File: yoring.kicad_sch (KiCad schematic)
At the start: 41 parts, among them J1 USB-C_USB4105-GF-A, J2 Conn_01x04_Pin, SW1 SW_MEC_5G, U1 ESP32C3, U2 IS25LP016D-JLLE, U4 ICM-20602, U4 USBLC6-2SC6, U5 ICM-20602, U6 ICM-20602, Y1 40.000MHZ

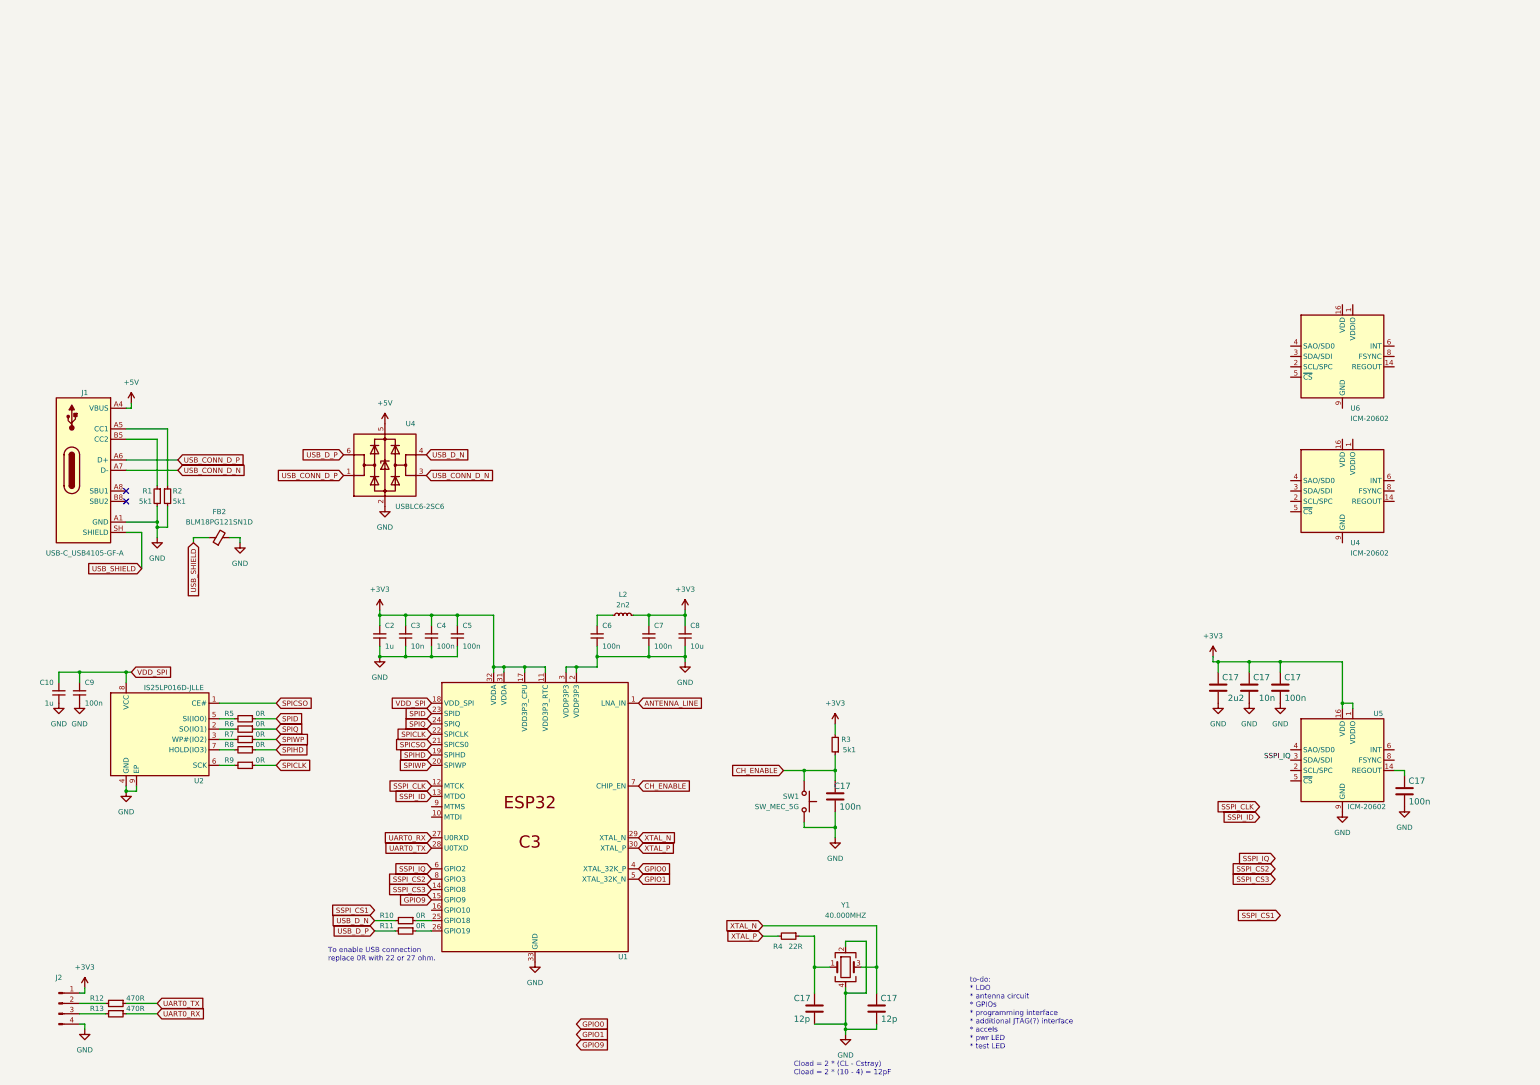
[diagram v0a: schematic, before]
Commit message: Reorganized schematic
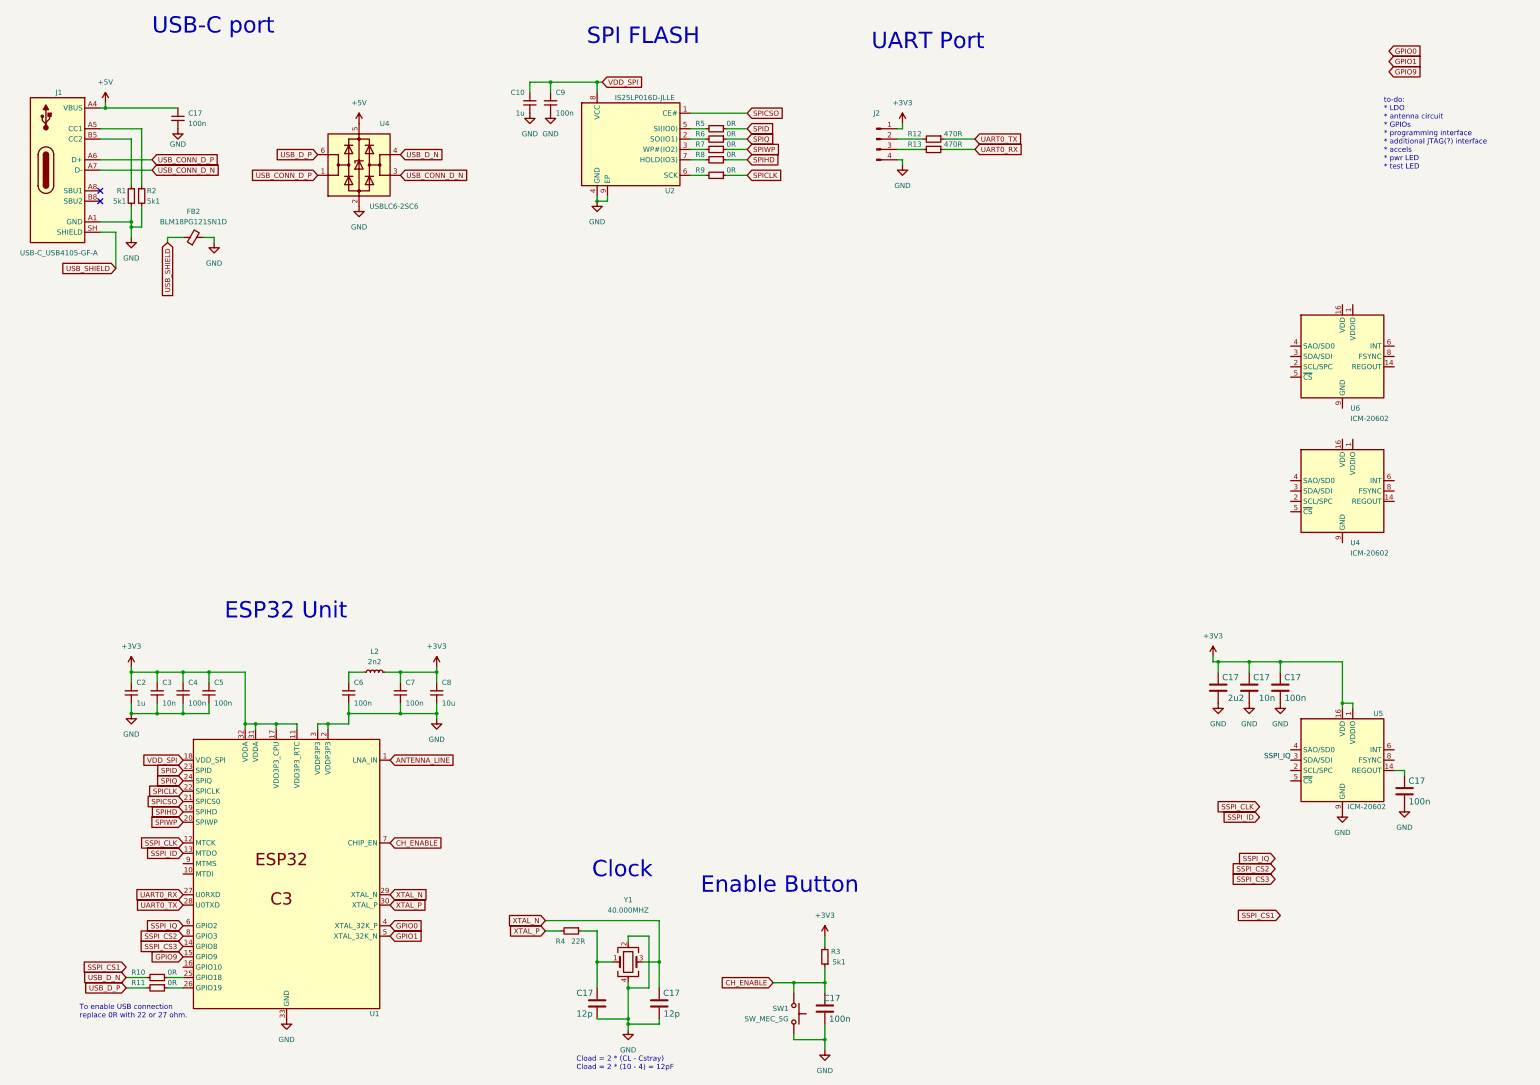
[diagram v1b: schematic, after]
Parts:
- added C17: 100n, symbol Device:C_Small
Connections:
- net +5V: now also C17.1
- net GND: now also C17.2
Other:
- note added: "Clock"
- note added: "ESP32 Unit"
- note added: "Enable Button"
- note added: "SPI FLASH"
- note added: "UART Port"
- note added: "USB-C port"
- moved on the sheet: C10, C17, C2, C3, C4, C5, C6, C7, C8, C9, FB2, J1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

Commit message: Finished schemtic
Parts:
- removed FB2: BLM18PG121SN1D, Inductor_SMD:L_0603_1608Metric, symbol Device:FerriteBead_Small
- removed J2: Conn_01x04_Pin, symbol Connector:Conn_01x04_Pin
- removed R13: 470R, symbol Device:R_Small
- added AE2: ACAG0301-2450-T, iridium-footprints:USB-C_GCT_USB4105-GF-A, symbol iridiumMisc:ACAG0301-2450-T
- added C17 (x2): 10n, Capacitor_SMD:C_0402_1005Metric_Pad0.74x0.62mm_HandSolder, symbol iridiumCapacitorsSMD:C_0402
- added C17 (x2): 2u2, Capacitor_SMD:C_0402_1005Metric_Pad0.74x0.62mm_HandSolder, symbol iridiumCapacitorsSMD:C_0402
- added C17 (x5): 100n, Capacitor_SMD:C_0402_1005Metric_Pad0.74x0.62mm_HandSolder, symbol iridiumCapacitorsSMD:C_0402
- added C26, C28, C30, C31: 100n, Capacitor_SMD:C_0402_1005Metric_Pad0.74x0.62mm_HandSolder, symbol Device:C_Small
- added C27, C29: 10u, Capacitor_SMD:C_0603_1608Metric_Pad1.08x0.95mm_HandSolder, symbol Device:C_Small
- added C33, C34: 3p3, Capacitor_SMD:C_0402_1005Metric_Pad0.74x0.62mm_HandSolder, symbol Device:C_Small
- added D1, D2: Green, LED_SMD:LED_0603_1608Metric_Pad1.05x0.95mm_HandSolder, symbol Device:LED_Small
- added J2, J3: Conn_01x05, Connector_PinHeader_2.54mm:PinHeader_1x05_P2.54mm_Vertical, symbol Connector_Generic:Conn_01x05
- added L1, L3: 2n2, Inductor_SMD:L_0402_1005Metric_Pad0.77x0.64mm_HandSolder, symbol Device:L_Small
- added R14, R15: 1k2, Resistor_SMD:R_0402_1005Metric_Pad0.72x0.64mm_HandSolder, symbol Device:R_Small
- added R16: 22R, Resistor_SMD:R_0402_1005Metric_Pad0.72x0.64mm_HandSolder, symbol Device:R_Small
- added R17, R18: 470R, Resistor_SMD:R_0402_1005Metric_Pad0.72x0.64mm_HandSolder, symbol Device:R_Small
- added SW2: SW_MEC_5G, Button_Switch_THT:SW_PUSH_6mm_H5mm, symbol Switch:SW_MEC_5G
- added U4: USBLC6-2SC6, Package_TO_SOT_SMD:SOT-23-6, symbol Power_Protection:USBLC6-2SC6
- added U7: AMS1117-3.3, Package_TO_SOT_SMD:SOT-223-3_TabPin2, symbol Regulator_Linear:AMS1117-3.3
- C10, C2: value 1u -> 10u; footprint (none) -> Capacitor_SMD:C_0603_1608Metric_Pad1.08x0.95mm_HandSolder
- C17: footprint iridium-footprints:0402-cap -> Capacitor_SMD:C_0402_1005Metric_Pad0.74x0.62mm_HandSolder
- C17, C4, C5, C6, C7, C9: footprint (none) -> Capacitor_SMD:C_0402_1005Metric_Pad0.74x0.62mm_HandSolder
- C3: value 10n -> 100n; footprint (none) -> Capacitor_SMD:C_0402_1005Metric_Pad0.74x0.62mm_HandSolder
- C8: footprint (none) -> Capacitor_SMD:C_0603_1608Metric_Pad1.08x0.95mm_HandSolder
- J1: footprint antmicro-footprints:GCT_USB4105-GF-A -> iridium-footprints:USB-C_GCT_USB4105-GF-A; symbol USBDVIHDMIConnectors:USB-C_USB4105-GF-A -> iridiumConnectors:USB-C_USB4105-GF-A
- L2: footprint (none) -> Inductor_SMD:L_0402_1005Metric_Pad0.77x0.64mm_HandSolder
- R1, R10, R11, R2, R3, R4, R5, R6, R7, R8, R9: footprint (none) -> Resistor_SMD:R_0402_1005Metric_Pad0.72x0.64mm_HandSolder
- R12: value 470R -> 5k1; footprint (none) -> Resistor_SMD:R_0402_1005Metric_Pad0.72x0.64mm_HandSolder
- SW1: footprint (none) -> Button_Switch_THT:SW_PUSH_6mm_H5mm
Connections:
- net +3V3: now also R12.2, U4.16 (VDD), U6.16 (VDD), C17.2, C17.2, C17.2, C17.2, C26.1, C27.1, J2.1 (Pin_1), J3.1 (Pin_1), R14.1, R15.1, U7.2 (VO); no longer C17.2, U5.1 (VDDIO)
- net +5V: now also C30.1, L1.1, U4.5 (VBUS)
- net ANTENNA_LINE: now also C33.1, L3.1
- net GND: now also U4.10 (GND), U4.11 (GND), U4.12 (GND), U4.13 (GND), U4.15 (GND), U4.9 (GND), U6.10 (GND), U6.11 (GND), U6.12 (GND), U6.13 (GND), U6.15 (GND), U6.9 (GND), C17.1, C17.1, C17.1, C17.1, C17.1, C17.1, C17.1, C17.1, C17.1, C26.2, C27.2, C28.2, C29.2, C30.2, C31.2, C33.2, C34.2, D1.1 (K), J2.5 (Pin_5), J3.5 (Pin_5), SW2.1 (A), SW2.2 (A), U4.2 (GND), U7.1 (GND)
- net GPIO0: now also J2.2 (Pin_2)
- net GPIO1: now also J2.3 (Pin_3)
- net GPIO9: now also R12.1, C17.2, SW2.3 (B), SW2.4 (B)
- net SSPI_CLK: now also U4.2 (SCL/SPC), U5.2 (SCL/SPC), U6.2 (SCL/SPC), R16.2; no longer U1.12 (MTCK)
- net SSPI_CS1: now also U1.16 (GPIO10), U6.5 (~{CS})
- net SSPI_CS2: now also U4.5 (~{CS})
- net SSPI_CS3: now also U5.5 (~{CS})
- net SSPI_ID: now also U4.3 (SDA/SDI), U5.3 (SDA/SDI), U6.3 (SDA/SDI)
- net SSPI_IQ: now also U4.4 (SAO/SD0), U5.4 (SAO/SD0), U6.4 (SAO/SD0); no longer U5.3 (SDA/SDI)
- net UART0_RX: now also R17.2, U4.4 (I/O2); no longer U1.27 (U0RXD)
- net UART0_TX: now also R18.2, U4.6 (I/O1); no longer R12.1, U1.28 (U0TXD)
- net at U4.1 (VDDIO): now also C17.2
- net at U4.14 (REGOUT): now also C17.2
- net GPIO5: now reaches U1.10 (MTDI)
- net GPIO5: now also D2.1 (K)
- net GPIO4: now reaches U1.9 (MTMS)
- net GPIO4: now also J2.4 (Pin_4)
- net at U6.1 (VDDIO): now also C17.2
- net at U6.14 (REGOUT): now also C17.2
- net USB_SHIELD: no longer names the net of J1.SH (SHIELD)
- new net: R16.1, U1.12 (MTCK)
- new net: R17.1, U1.27 (U0RXD)
- new net: R18.1, U1.28 (U0TXD)
- new net: C17.2, U5.1 (VDDIO)
- new net: D1.2 (A), R14.2
- new net: AE2.1, C34.1, L3.2
- new net: D2.2 (A), R15.2
- new net 5V_FILTERED: C28.1, C29.1, C31.1, J3.2 (Pin_2), L1.2, U7.3 (VI)
- new net UART0_RX_CONN: J3.4 (Pin_4), U4.3 (I/O2)
- new net UART0_TX_CONN: J3.3 (Pin_3), U4.1 (I/O1)
- no-connect marks 2 -> 9
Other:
- note added: "Antenna"
- note added: "Boot Select"
- note added: "GPIOs"
- note added: "PWR LED"
- note added: "SPI Sensors"
- note added: "Test LED"
- note added: "replace with NCV1117ST33T3G"
- note removed: "to-do: * LDO * antenna circuit * GPIOs * programming interface * additional JTAG(?) interface * accels * pwr LED * test LED"
- moved on the sheet: C17, U4, U5, U6

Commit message: Added layout
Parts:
- removed J2: Conn_01x05, Connector_PinHeader_2.54mm:PinHeader_1x05_P2.54mm_Vertical, symbol Connector_Generic:Conn_01x05
- removed R10, R11, R6, R7, R8, R9: 0R, Resistor_SMD:R_0402_1005Metric_Pad0.72x0.64mm_HandSolder, symbol Device:R_Small
- removed SW1, SW2: SW_MEC_5G, Button_Switch_THT:SW_PUSH_6mm_H5mm, symbol Switch:SW_MEC_5G
- added D3: Green, LED_SMD:LED_0603_1608Metric_Pad1.05x0.95mm_HandSolder, symbol Device:LED_Small
- added SW1, SW2: SW_MEC_5E, Button_Switch_THT:SW_PUSH_6mm_H5mm, symbol Switch:SW_MEC_5E
- AE2: footprint iridium-footprints:USB-C_GCT_USB4105-GF-A -> iridium-footprints:ANTC3216X130N
- R5: value 0R -> 1k2
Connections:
- net +3V3: now also C17.2, C17.2, C17.2, R5.1, U4.1 (VDDIO), U5.1 (VDDIO), U6.1 (VDDIO)
- net +5V: now also J3.2 (Pin_2)
- net 5V_FILTERED: no longer J3.2 (Pin_2)
- net CH_ENABLE: now also SW2.3 (K), SW2.4 (A)
- net GND: now also SW1.1, SW1.2, SW2.1, SW2.2; no longer U1.2 (VDDP3P3), U1.3 (VDDP3P3)
- net GPIO4: now also D3.1 (K)
- net GPIO9: now also SW1.3 (K), SW1.4 (A)
- net SPICLK: now also U2.6 (SCK)
- net SPID: now also U2.5 (SI(IO0)); no longer R5.1
- net SPIHD: now also U2.7 (HOLD(IO3))
- net SPIQ: now also U2.2 (SO(IO1))
- net SPIWP: now also U2.3 (WP#(IO2))
- net UART0_RX: now also U4.6 (I/O1); no longer U4.4 (I/O2)
- net UART0_RX_CONN: now also J3.3 (Pin_3), U4.1 (I/O1); no longer J3.4 (Pin_4), U4.3 (I/O2)
- net UART0_TX: now also U4.4 (I/O2); no longer U4.6 (I/O1)
- net UART0_TX_CONN: now also J3.4 (Pin_4), U4.3 (I/O2); no longer J3.3 (Pin_3), U4.1 (I/O1)
- net USB_CONN_D_N: now also U4.1 (I/O1); no longer U4.3 (I/O2)
- net USB_CONN_D_P: now also U4.3 (I/O2); no longer U4.1 (I/O1)
- net USB_D_N: now also U1.25 (GPIO18), U4.6 (I/O1); no longer U4.4 (I/O2)
- net USB_D_P: now also U1.26 (GPIO19), U4.4 (I/O2); no longer U4.6 (I/O1)
- net at R5.2: now also D3.2 (A); no longer U2.5 (SI(IO0))
- net ANTENNA_OUT: now reaches AE2.1, C34.1, L3.2
- net at C6.2, L2.1: now also U1.2 (VDDP3P3), U1.3 (VDDP3P3)
- net GPIO0: no longer names the net of U1.4 (XTAL_32K_P)
- net GPIO1: no longer names the net of U1.5 (XTAL_32K_N)
- no-connect marks 9 -> 11
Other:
- note removed: "GPIOs"
- moved on the sheet: AE2, D2, R15

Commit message: Added rectangle boxes for grouping components to schematic
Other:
- note added: "Power section"
- moved on the sheet: AE2, C10, C17, C2, C26, C27, C28, C29, C3, C30, C31, C33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
